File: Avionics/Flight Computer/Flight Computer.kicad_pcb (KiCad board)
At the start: 4 copper layers, 50 x 40 mm, 178 parts, among them J1 ERF8-040-05.0-S-DV-K, J2 ERF8-040-05.0-S-DV-K, J3 473460001, J4 734120110, J5 0734120110, J6 734120110, U1 CC1310F128RGZR, U12 ATSAME70Q21A-AN, U2 CC1190RGVR, U3 CC2650F128RGZR, U4 CC2592RGVR, U5 MPU-9250, U7 LPS25HB, U8 MAX17243, U9 MAX-M8W, Y1 9HT11-32.768KDZB-T, Y2 7V-16.000MAHJ-T, Y3 XRCGB24M000F2P00R0, Y5 XRCGB24M000F2P00R0

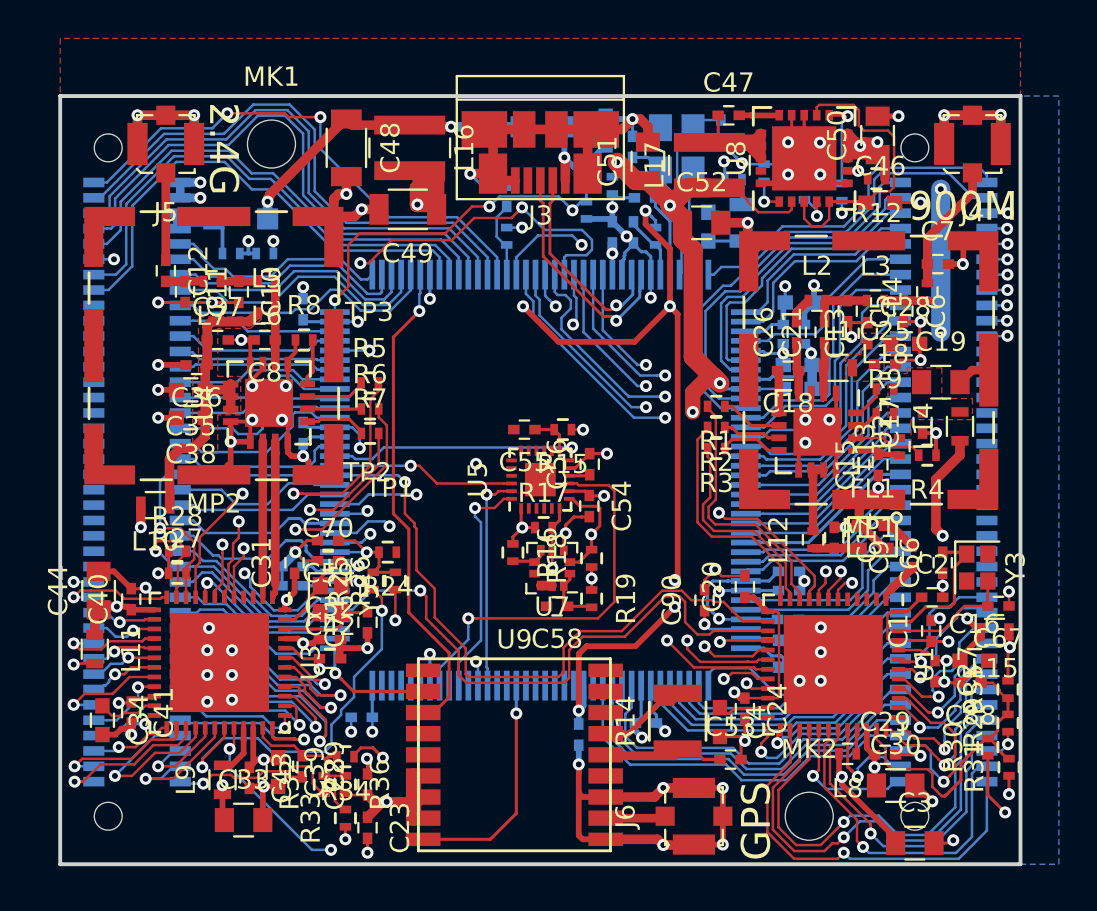
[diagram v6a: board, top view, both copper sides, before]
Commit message: Finished routing and DRC check.
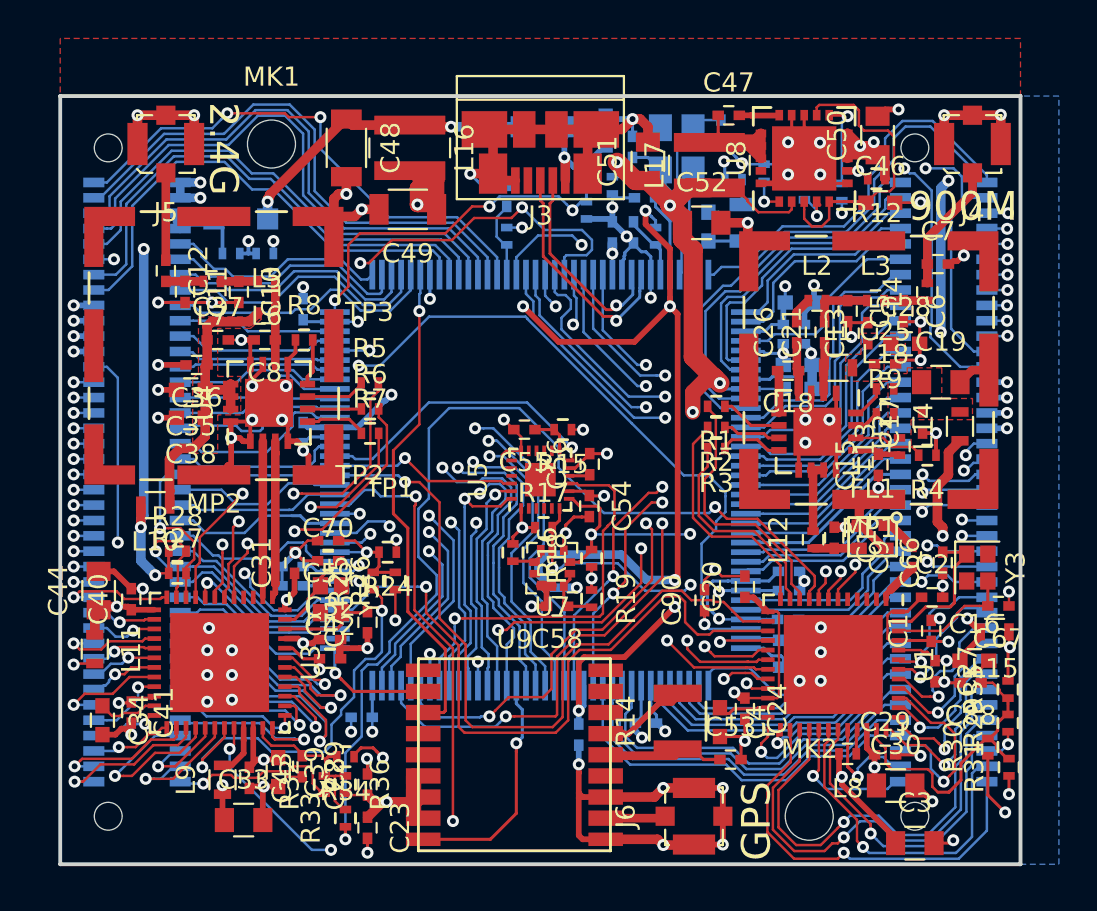
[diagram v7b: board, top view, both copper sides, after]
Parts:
- moved TP2 0.43 mm to (65.6, 106.8)
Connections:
- J1 pad 18: Net-(J1-Pad18) -> GND
- J1 pad 20: Net-(J1-Pad20) -> GND
- J1 pad 22: Net-(J1-Pad22) -> GND
- J1 pad 24: Net-(J1-Pad24) -> GND
- J1 pad 26: Net-(J1-Pad26) -> /Connectors/PB12
- J1 pad 28: Net-(J1-Pad28) -> /Connectors/PD25
- J1 pad 30: Net-(J1-Pad30) -> /Connectors/PD26
- J1 pad 32: Net-(J1-Pad32) -> /Connectors/PC6
- J1 pad 34: Net-(J1-Pad34) -> /Connectors/PD24
- J1 pad 36: Net-(J1-Pad36) -> /Connectors/PA24
- J1 pad 38: Net-(J1-Pad38) -> /Connectors/PC5
- J1 pad 40: Net-(J1-Pad40) -> /Connectors/PA25
- J1 pad 42: Net-(J1-Pad42) -> /Connectors/PA26
- J1 pad 44: Net-(J1-Pad44) -> /Connectors/PA11
- J1 pad 46: Net-(J1-Pad46) -> /Connectors/PA12
- J1 pad 48: Net-(J1-Pad48) -> /Connectors/PA27
- J1 pad 50: Net-(J1-Pad50) -> /Connectors/PD28
- J1 pad 52: Net-(J1-Pad52) -> /CPU_RESET_EXT
- J2 pad 23: Net-(J2-Pad23) -> /Power-Good
- J2 pad 25: Net-(J2-Pad25) -> /Power-~SHDN~
- J2 pad 27: Net-(J2-Pad27) -> GND
- J2 pad 29: Net-(J2-Pad29) -> GND
- J2 pad 31: Net-(J2-Pad31) -> GND
- J2 pad 33: Net-(J2-Pad33) -> GND
- J2 pad 35: Net-(J2-Pad35) -> /Connectors/PA14
- J2 pad 37: Net-(J2-Pad37) -> /Connectors/PA15
- J2 pad 39: Net-(J2-Pad39) -> /Connectors/AUX_SCL
- J2 pad 41: Net-(J2-Pad41) -> /Connectors/AUX_SDA
- J2 pad 43: Net-(J2-Pad43) -> /Connectors/900-DIO-10
- J2 pad 45: Net-(J2-Pad45) -> /Connectors/900-DIO-11
- J2 pad 47: Net-(J2-Pad47) -> /Connectors/900-DIO-12
- J2 pad 49: Net-(J2-Pad49) -> /Connectors/900-DIO-13
- J2 pad 51: Net-(J2-Pad51) -> /Connectors/900-DIO-14
- J2 pad 53: Net-(J2-Pad53) -> /Connectors/900-DIO-15
- U1 pad 16: /900MHz Radio/DIO-10 -> /Connectors/900-DIO-10
- U1 pad 17: /900MHz Radio/DIO-11 -> /Connectors/900-DIO-11
- U1 pad 18: /900MHz Radio/DIO-12 -> /Connectors/900-DIO-12
- U1 pad 19: /900MHz Radio/DIO-13 -> /Connectors/900-DIO-13
- U1 pad 20: /900MHz Radio/DIO-14 -> /Connectors/900-DIO-14
- U1 pad 21: /900MHz Radio/DIO-15 -> /Connectors/900-DIO-15
- U12 pad 49: /GNC_Processor/PA15 -> /Connectors/PA15
- U12 pad 51: /GNC_Processor/PA14 -> /Connectors/PA14
- U12 pad 52: /GNC_Processor/PD25 -> /Connectors/PD25
- U12 pad 53: /GNC_Processor/PD26 -> /Connectors/PD26
- U12 pad 54: /GNC_Processor/PC6 -> /Connectors/PC6
- U12 pad 55: /GNC_Processor/PD24 -> /Connectors/PD24
- U12 pad 56: /GNC_Processor/PA24 -> /Connectors/PA24
- U12 pad 58: /GNC_Processor/PC5 -> /Connectors/PC5
- U12 pad 59: /GNC_Processor/PA25 -> /Connectors/PA25
- U12 pad 62: /GNC_Processor/PA26 -> /Connectors/PA26
- U12 pad 64: /GNC_Processor/PA11 -> /Connectors/PA11
- U12 pad 68: /GNC_Processor/PA12 -> /Connectors/PA12
- U12 pad 70: /GNC_Processor/PA27 -> /Connectors/PA27
- U12 pad 71: /GNC_Processor/PD28 -> /Connectors/PD28
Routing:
- net /900_RESET_CPU: track 5.41 -> 56.5 mm, vias 2 -> 3
- net /2.4_RESET_900: track 8.33 -> 51.3 mm
- net /GNC_Processor/VBATT: track 4.45 -> 45.7 mm, vias 2 -> 3
- net /Connectors/PD25: track 0.00 -> 39.7 mm, vias 0 -> 2
- net /Connectors/PD26: track 0.00 -> 39.1 mm, vias 0 -> 2
- net /Connectors/PC6: track 0.00 -> 38.4 mm, vias 0 -> 2
- net /Connectors/PD24: track 0.00 -> 37.8 mm, vias 0 -> 2
- net /Connectors/PA24: track 0.00 -> 37.5 mm, vias 0 -> 2
- net /Connectors/PC5: track 0.00 -> 37.2 mm, vias 0 -> 2
- net /Connectors/PA25: track 0.00 -> 37.1 mm, vias 0 -> 2
- net /Connectors/PA26: track 0.00 -> 33.8 mm, vias 0 -> 2
- net /900M-Tx: track 1.60 -> 34.5 mm, vias 1 -> 3
- net /900M-Rx: track 1.72 -> 34.1 mm, vias 1 -> 3
- net /Connectors/PA11: track 0.00 -> 32.1 mm, vias 0 -> 2
- net /Connectors/PA12: track 0.00 -> 31.6 mm, vias 0 -> 2
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
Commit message: Cleaned up routing details and plane continuity problems.
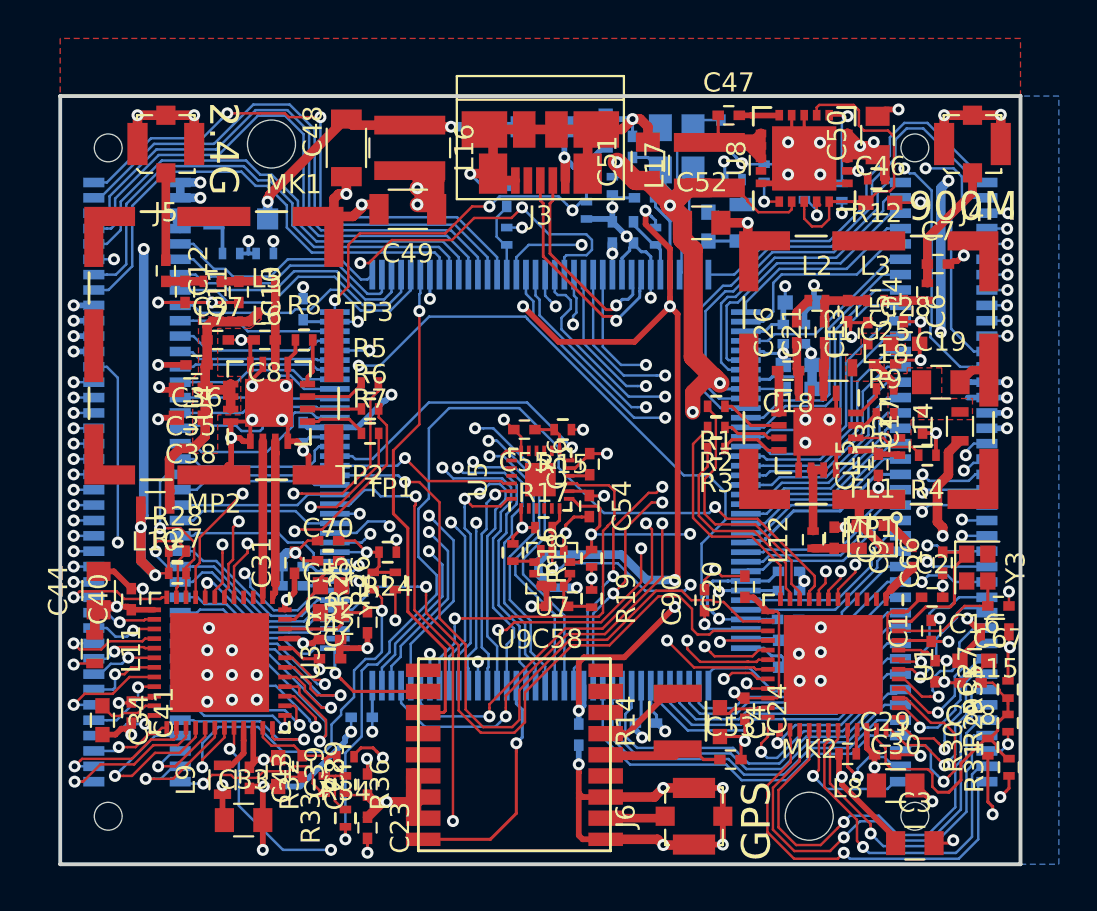
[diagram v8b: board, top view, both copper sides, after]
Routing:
- net GND: track 257.2 -> 266.9 mm, vias 96 -> 100
- net /Connectors/PB6: track 17.0 -> 21.2 mm
- net /Connectors/PD2: track 32.6 -> 29.7 mm
- net /Connectors/PD5: track 36.1 -> 33.2 mm
- net /Connectors/PD3: track 34.5 -> 31.5 mm
- net /Connectors/PD4: track 35.0 -> 32.1 mm
- net +3V3: track 121.1 -> 123.9 mm
- net /900MHz Radio/VDDS_CC1310: track 45.3 -> 47.9 mm
- net /CPU_RESET_900: track 34.5 -> 32.1 mm
- net /Connectors/PD1: track 31.2 -> 29.1 mm
- net /Connectors/PC21: track 27.5 -> 29.3 mm
- net /Connectors/PB12: track 26.6 -> 28.3 mm
- net /900MHz Radio/VDD_CC1190: track 0.00 -> 1.71 mm
- net /900_RESET_CPU: track 56.5 -> 54.8 mm
- net /Connectors/PA15: track 30.2 -> 31.9 mm
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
